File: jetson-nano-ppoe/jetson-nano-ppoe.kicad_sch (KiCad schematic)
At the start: 19 parts, among them J1 Conn_01x02, J2 Conn_02x05_Odd_Even, J3 Conn_02x02_Odd_Even, J4 Conn_02x06_Odd_Even, J5 Conn_01x06, Q2 Q_PMOS_GSD, Q4 Q_NMOS_DUAL

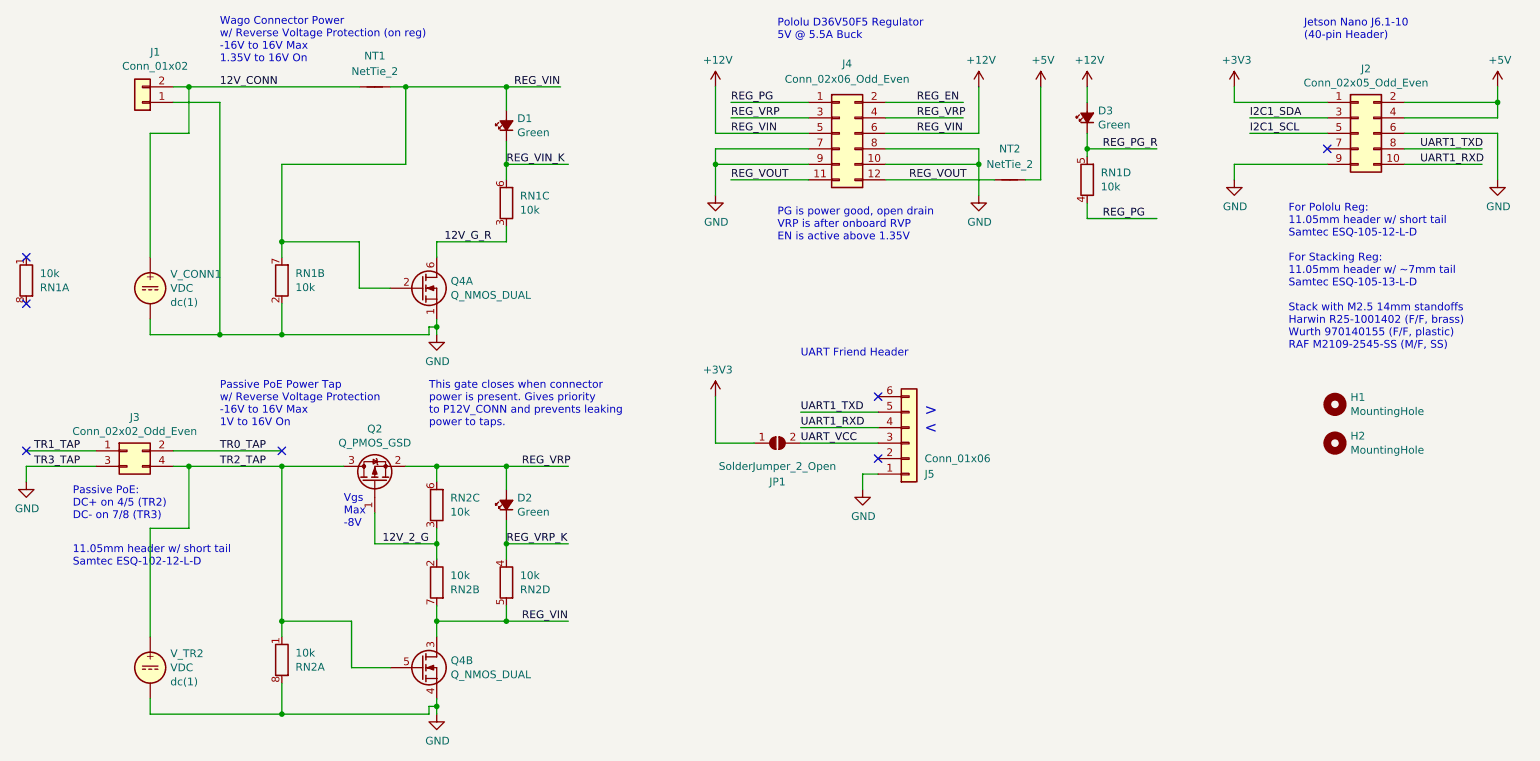
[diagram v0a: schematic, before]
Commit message: add gigablox-nano-rvp and simplify jetson-nano-ppoe
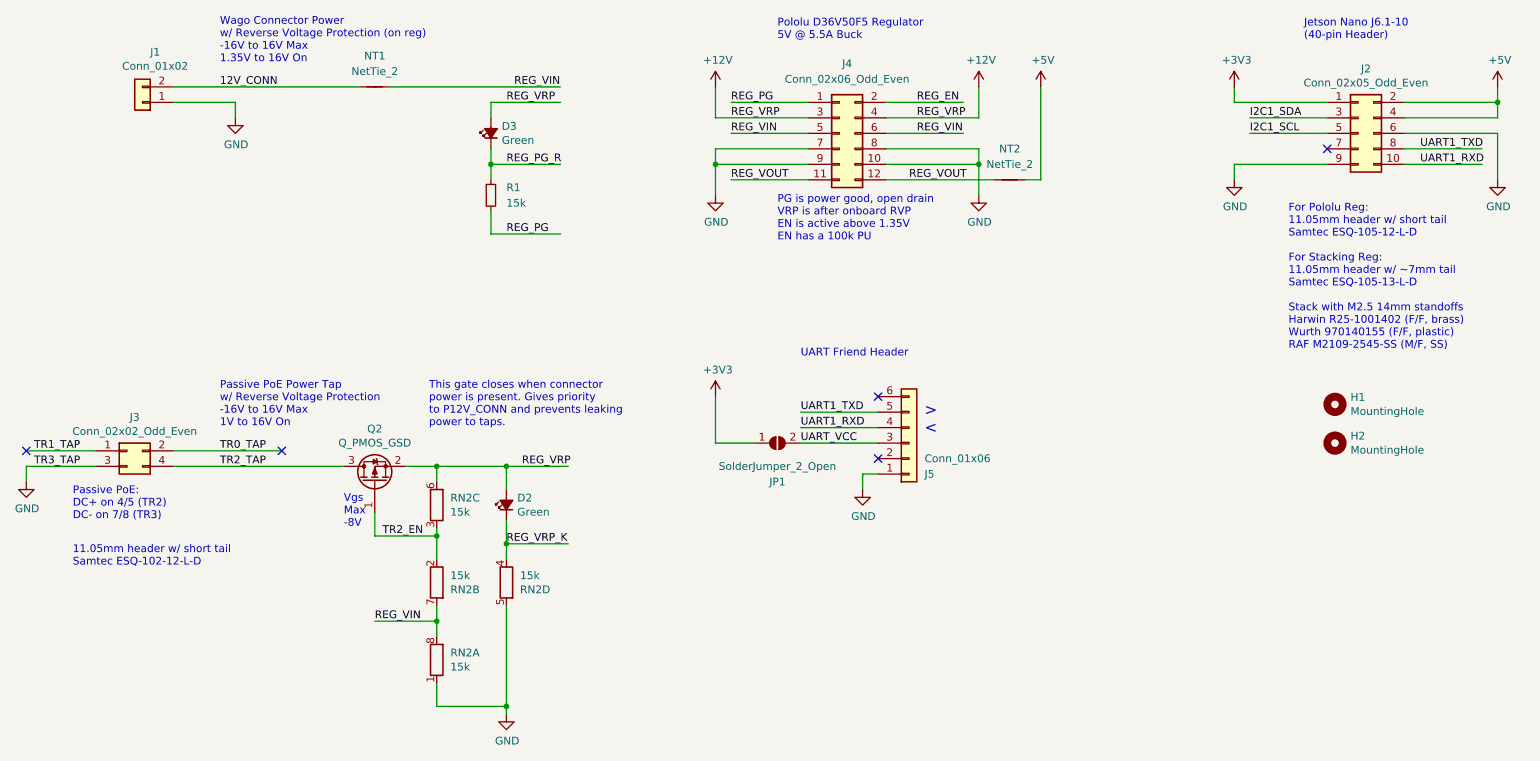
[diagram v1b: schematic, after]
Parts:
- removed D1: Green, LED_SMD:LED_0603_1608Metric, symbol Device:LED_Small_Filled
- removed Q4: Q_NMOS_DUAL, Package_TO_SOT_SMD:SOT-23-6, symbol frc-on-ftc-hw-special:Q_NMOS_DUAL
- removed RN1: 10k, Resistor_SMD:R_Array_Convex_4x1206, symbol frc-on-ftc-hw-special:R_Pack04_SMD_Split
- removed V_CONN1, V_TR2: VDC, symbol Simulation_SPICE:VDC
- added R1: 15k, Resistor_SMD:R_0805_2012Metric, symbol Device:R_Small
- RN2: value 10k -> 15k; Mfg PN YC164-JR-0710KL -> YC164-JR-0715KL
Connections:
- net REG_VRP is gone; now on net +12V: D2.2 (A), J4.3 (Pin_3), J4.4 (Pin_4), Q2.2 (S), RN2.6 (R1.2)
- net +12V: no longer J4.5 (Pin_5), J4.6 (Pin_6), NT1.2, RN2.5 (R1.2), RN2.7 (R1.2)
- net GND: now also RN2.1 (R1.1), RN2.5 (R1.2); no longer RN2.8 (R1.2)
- net REG_PG: now also R1.2
- net REG_PG_R: now also R1.1
- net TR2_TAP: no longer RN2.1 (R1.1)
- net 12V_2_G renamed TR2_EN
- new net REG_VIN: J4.5 (Pin_5), J4.6 (Pin_6), NT1.2, RN2.7 (R1.2), RN2.8 (R1.2)
- no-connect marks 7 -> 5
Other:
- note added: "PG is power good, open drain VRP is after onboard RVP EN is active above 1.35V EN has a 100k PU"
- note removed: "PG is power good, open drain VRP is after onboard RVP EN is active above 1.35V"
- moved on the sheet: D3, RN2A

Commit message: gigablox-nano-rvp and jetson-nano-ppoe boms
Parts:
- D2, D3: Mfg (none) -> Lite-On; Mfg PN (none) -> LTST-C190GKT
- J1: Mfg (none) -> Wago; Mfg PN (none) -> 250-202
- J2: Mfg (none) -> Samtec; Mfg Pn (none) -> ESQ-105-13-L-D
- J3: Mfg (none) -> Samtec; Mfg PN (none) -> ESQ-102-12-L-D
- R1: Mfg (none) -> uni-royal; Mfg PN (none) -> 0805W8F1502T5E
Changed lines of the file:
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@@
+      (effects (font (size 1.27 1.27)) hide)
+    )
+    (property "Mfg" "Samtec" (id 4) (at 242.57 82.55 0)
+      (effects (font (size 1.27 1.27)) hide)
+    )
+    (property "Mfg Pn" "ESQ-105-13-L-D" (id 5) (at 242.57 82.55 0)
       (effects (font (size 1.27 1.27)) hide)
     )
@@
       (effects (font (size 1.27 1.27)) hide)
     )
+    (property "Mfg" "Wago" (id 4) (at 43.18 77.47 0)
+      (effects (font (size 1.27 1.27)) hide)
+    )
+    (property "Mfg PN" "250-202" (id 5) (at 43.18 77.47 0)
+      (effects (font (size 1.27 1.27)) hide)
+    )
     (pin "1")
     (pin "2")
@@
       (effects (font (size 1.27 1.27)) hide)
     )
+    (property "Mfg" "Samtec" (id 4) (at 40.64 134.62 0)
+      (effects (font (size 1.27 1.27)) hide)
+    )
+    (property "Mfg PN" "ESQ-102-12-L-D" (id 5) (at 40.64 134.62 0)
+      (effects (font (size 1.27 1.27)) hide)
+    )
     (pin "1")
     (pin "2")
@@
     )
     (property "Spice_Lib_File" "/Users/ihartwig/repos/KiCad-Spice-Library/Models/Diode/led.lib" (id 7) (at 102.87 143.51 0)
+      (effects (font (size 1.27 1.27)) hide)
+    )
+    (property "Mfg" "Lite-On" (id 8) (at 102.87 143.51 90)
+      (effects (font (size 1.27 1.27)) hide)
+    )
+    (property "Mfg PN" "LTST-C190GKT" (id 9) (at 102.87 143.51 90)
       (effects (font (size 1.27 1.27)) hide)
     )
@@
       (effects (font (size 1.27 1.27)) hide)
     )
+    (property "Mfg" "Lite-On" (id 8) (at 100.33 82.55 90)
+      (effects (font (size 1.27 1.27)) hide)
+    )
+    (property "Mfg PN" "LTST-C190GKT" (id 9) (at 100.33 82.55 90)
+      (effects (font (size 1.27 1.27)) hide)
+    )
     (pin "1")
     (pin "2")
@@
       (effects (font (size 1.27 1.27)) hide)
     )
+    (property "Mfg" "uni-royal" (id 4) (at 100.33 92.71 0)
+      (effects (font (size 1.27 1.27)) hide)
+    )
+    (property "Mfg PN" "0805W8F1502T5E" (id 5) (at 100.33 92.71 0)
+      (effects (font (size 1.27 1.27)) hide)
+    )
